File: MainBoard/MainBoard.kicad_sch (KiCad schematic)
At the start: 56 parts, among them J2 Non-Inverting Input, J3 Inverting Input, J4 Output, J5 InvertedOutput, J6 Inverting Input, J7 Non-Inverting Input, J8 Output, J9 InvertedOutput, Q16 BC557, Q32 BC557

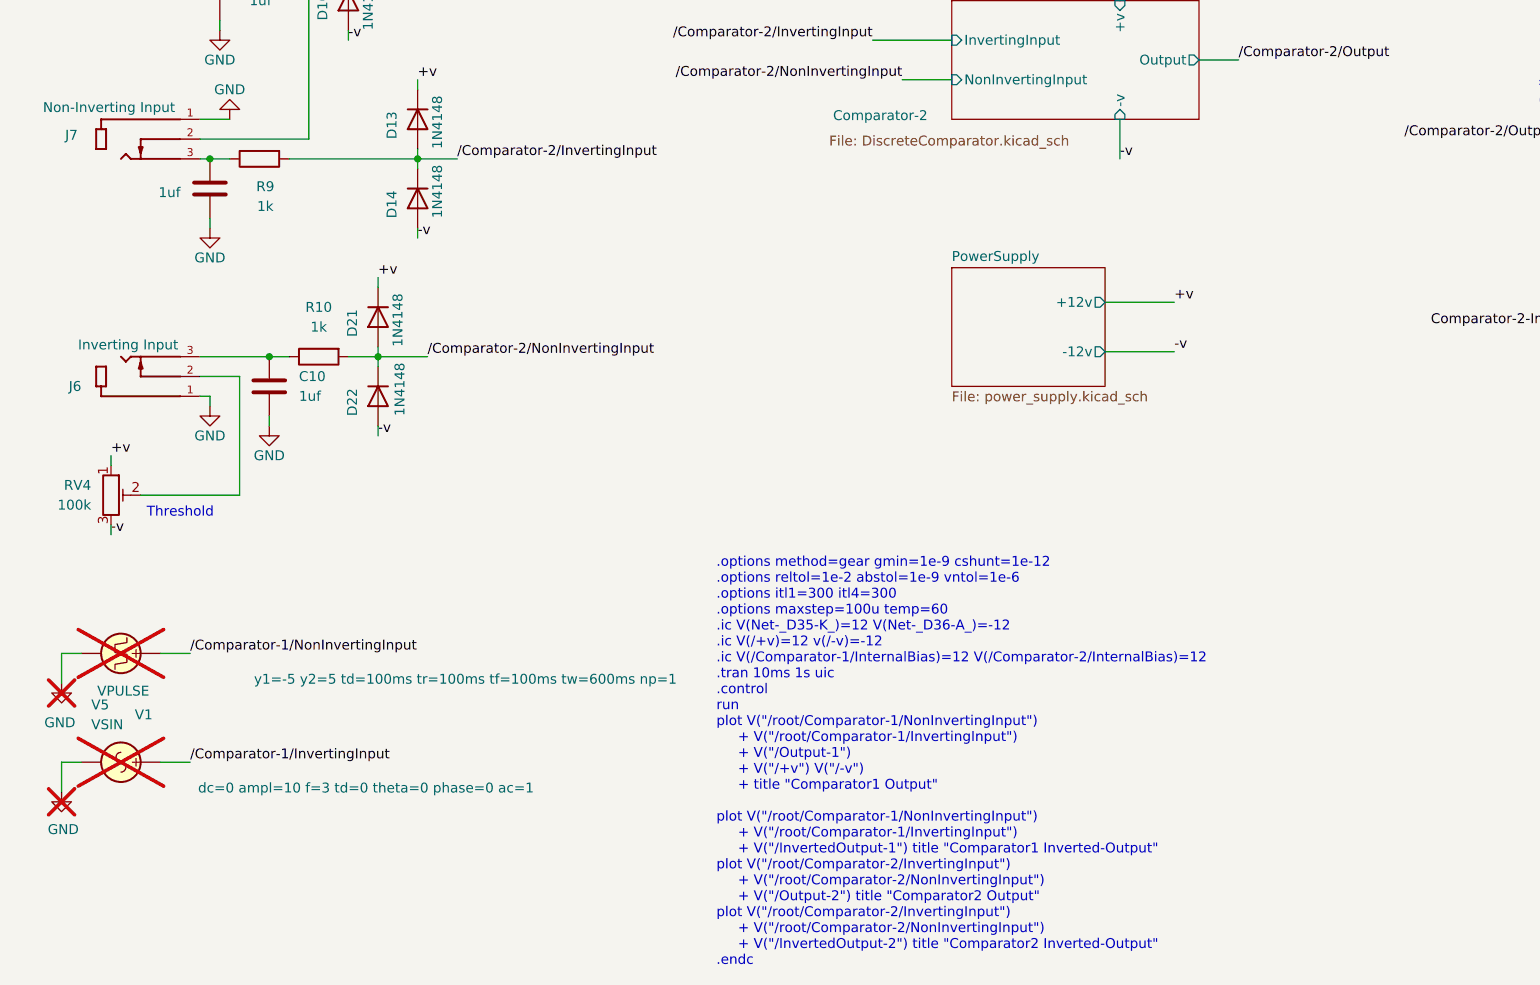
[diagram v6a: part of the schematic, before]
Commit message: updated input signal amplitude -- WIP window comparator testing [i.e, sine wave as threshold currently disabled
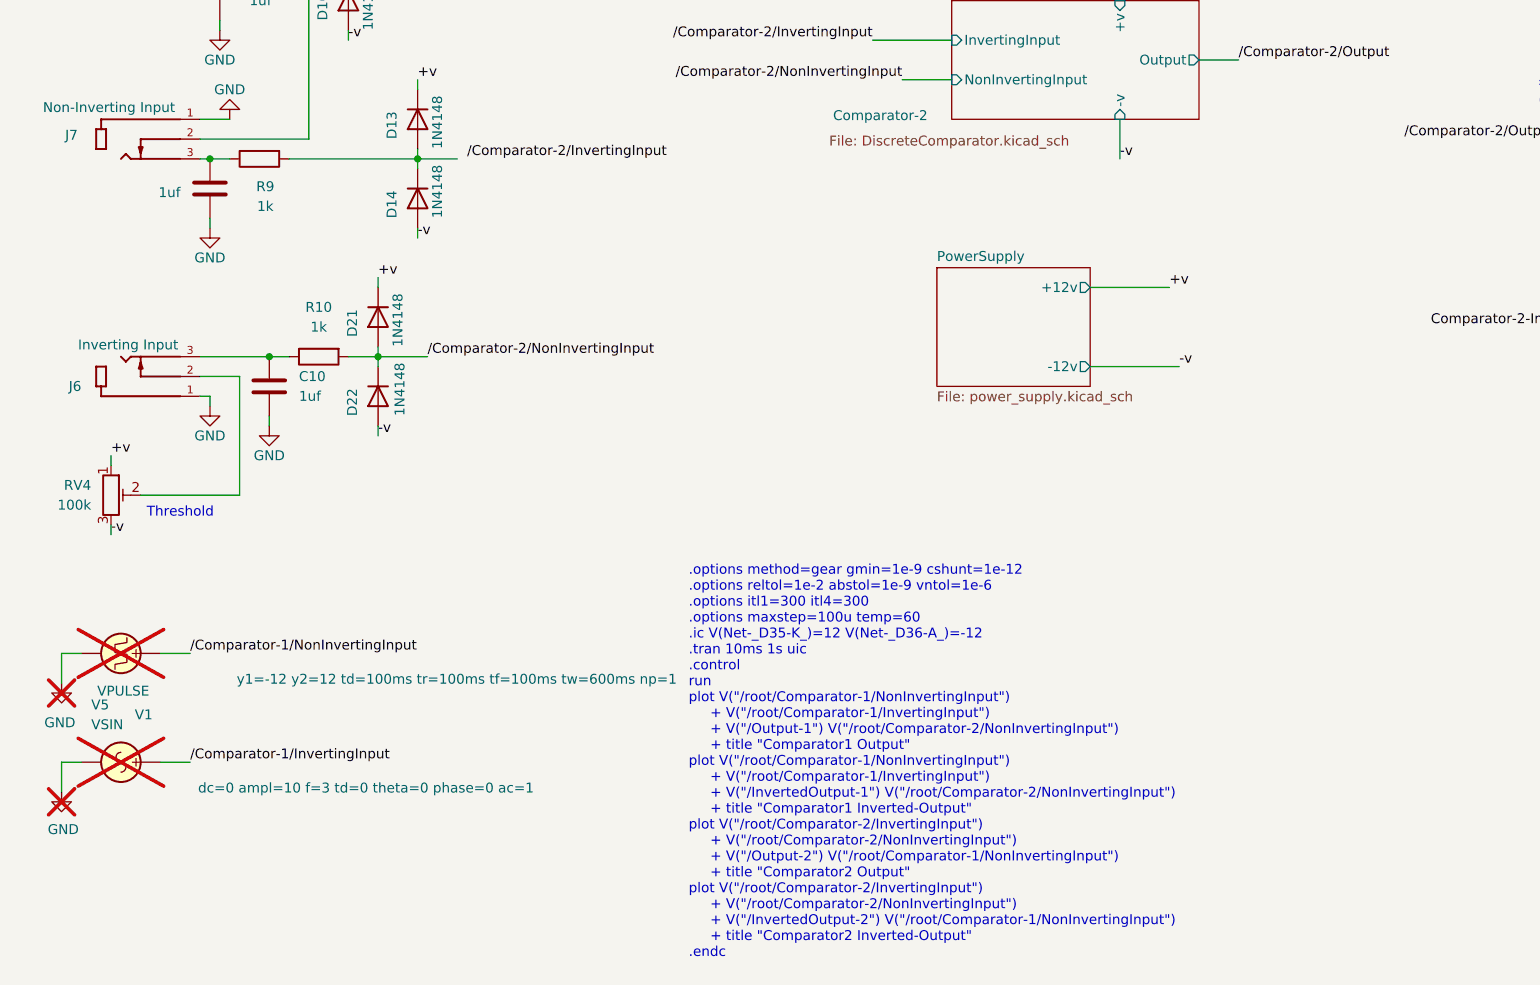
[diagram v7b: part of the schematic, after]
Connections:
- net /Comparator-2/InvertingInput: no longer D13.2 (A), D14.1 (K), R9.2
- new net: D13.2 (A), D14.1 (K), R9.2
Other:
- note added: ".options method=gear gmin=1e-9 cshunt=1e-12 .options reltol=1e-2 abstol=1e-9 vntol=1e-6 .options itl1=300 itl4=300 .options maxstep=100u temp=60 .ic V(Net-_D35-K_)=12 V(Net-_D36-A_)=-12 .tran 10ms 1s uic .control run plot V("/root/Comparator-1/NonInvertingInput") + V("/root/Comparator-1/InvertingInput") + V("/Output-1") V("/root/Comparator-2/NonInvertingInput") + title "Comparator1 Output" plot V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"
- note removed: ".options method=gear gmin=1e-9 cshunt=1e-12 .options reltol=1e-2 abstol=1e-9 vntol=1e-6 .options itl1=300 itl4=300 .options maxstep=100u temp=60 .ic V(Net-_D35-K_)=12 V(Net-_D36-A_)=-12 .ic V(/+v)=12 v(/-v)=-12 .ic V(/Comparator-1/InternalBias)=12 V(/Comparator-2/InternalBias)=12 .tran 10ms 1s uic .control run plot V("/root/Comparator-1/NonInvertingInput") + V("/root/Comparator-1/InvertingInput")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"
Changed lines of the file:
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@@
 		)
 	)
-	(text ".options method=gear gmin=1e-9 cshunt=1e-12 \n.options reltol=1e-2 abstol=1e-9 vntol=1e-6 \n.options itl1=300 itl4=300 \n.options maxstep=100u temp=60\n.ic V(Net-_D35-K_)=12 V(Net-_D36-A_)=-12 \n.ic V(/+v)=12 v(/-v)=-12 \n.ic V(/Comparator-1/InternalBias)=12 V(/Comparator-2/InternalBias)=12\n.tran 10ms 1s uic\n.control\nrun\nplot V(\"/root/Comparator-1/NonInvertingInput\") \n     + V(\"/root/Comparator-1/InvertingInput\") \n     + V(\"/Output-1\")\n     + V(\"/+v\") V(\"/-v\")\n     + title \"Comparator1 Output\" \n    \nplot V(\"/root/Comparator-1/NonInvertingInput\")\n     + V(\"/root/Comparator-1/InvertingInput\")\n     + V(\"/InvertedOutput-1\") title \"Comparator1 Inverted-Output\"\nplot V(\"/root/Comparator-2/InvertingInput\") \n     + V(\"/root/Comparator-2/NonInvertingInput\")   \n     + V(\"/Output-2\") title \"Comparator2 Output\" \nplot V(\"/root/Comparator-2/InvertingInput\")\n     + V(\"/root/Comparator-2/NonInvertingInput\") \n     + V(\"/InvertedOutput-2\") title \"Comparator2 Inverted-Output\"\n.endc"
+	(text ".options method=gear gmin=1e-9 cshunt=1e-12 \n.options reltol=1e-2 abstol=1e-9 vntol=1e-6 \n.options itl1=300 itl4=300 \n.options maxstep=100u temp=60\n.ic V(Net-_D35-K_)=12 V(Net-_D36-A_)=-12 \n.tran 10ms 1s uic\n.control\nrun\nplot V(\"/root/Comparator-1/NonInvertingInput\") \n     + V(\"/root/Comparator-1/InvertingInput\") \n     + V(\"/Output-1\") V(\"/root/Comparator-2/NonInvertingInput\")\n     + title \"Comparator1 Output\" \nplot V(\"/root/Comparator-1/NonInvertingInput\")\n     + V(\"/root/Comparator-1/InvertingInput\")\n     + V(\"/InvertedOutput-1\") V(\"/root/Comparator-2/NonInvertingInput\")\n     + title \"Comparator1 Inverted-Output\"\nplot V(\"/root/Comparator-2/InvertingInput\") \n     + V(\"/root/Comparator-2/NonInvertingInput\")   \n     + V(\"/Output-2\") V(\"/root/Comparator-1/NonInvertingInput\") \n     + title \"Comparator2 Output\" \nplot V(\"/root/Comparator-2/InvertingInput\")\n     + V(\"/root/Comparator-2/NonInvertingInput\") \n     + V(\"/InvertedOutput-2\") V(\"/root/Comparator-1/NonInvertingInput\") \n     + title \"Comparator2 Inverted-Output\"\n.endc"
 		(exclude_from_sim no)
-		(at 105.664 168.91 0)
+		(at 102.108 168.91 0)
 		(effects
 			(font
@@
 	(wire
 		(pts
+			(xy 153.67 107.95) (xy 163.83 107.95)
+		)
+		(stroke
+			(width 0)
+			(type default)
+		)
+	)
+	(wire
+		(pts
 			(xy 58.42 55.88) (xy 58.42 57.15)
 		)
@@
 	(wire
 		(pts
-			(xy 40.64 123.19) (xy 40.64 121.92)
+			(xy 153.67 118.11) (xy 165.1 118.11)
 		)
 		(stroke
@@
 	(wire
 		(pts
-			(xy 34.29 154.94) (xy 38.1 154.94)
+			(xy 40.64 123.19) (xy 40.64 121.92)
 		)
 		(stroke
@@
 	(wire
 		(pts
-			(xy 63.5 27.94) (xy 63.5 29.21)
+			(xy 34.29 154.94) (xy 38.1 154.94)
 		)
 		(stroke
@@
 	(wire
 		(pts
-			(xy 27.94 129.54) (xy 27.94 130.81)
+			(xy 63.5 27.94) (xy 63.5 29.21)
 		)
 		(stroke
@@
 	(wire
 		(pts
-			(xy 217.17 78.74) (xy 217.17 81.28)
+			(xy 27.94 129.54) (xy 27.94 130.81)
 		)
 		(stroke
@@
 	(wire
 		(pts
-			(xy 155.575 109.855) (xy 164.465 109.855)
+			(xy 217.17 78.74) (xy 217.17 81.28)
 		)
 		(stroke
@@
 	(wire
 		(pts
-			(xy 155.575 116.205) (xy 164.465 116.205)
-		)
-		(stroke
-			(width 0)
-			(type default)
-		)
-	)
-	(wire
-		(pts
 			(xy 44.45 119.38) (xy 39.37 119.38)
 		)
@@
 	)
 	(label "+v"
-		(at 164.465 109.855 0)
+		(at 163.83 107.95 0)
 		(effects
 			(font
@@
 	)
 	(label "{slash}Comparator-2{slash}InvertingInput"
-		(at 72.39 91.44 0)
+		(at 73.66 91.44 0)
 		(effects
 			(font
@@
 	)
 	(label "-v"
-		(at 164.465 116.205 0)
+		(at 165.1 118.11 0)
 		(effects
 			(font
@@
 			)
 		)
-		(property "Sim.Params" "Rtot=100k w=0.3"
+		(property "Sim.Params" "Rtot=100k w=0.7"
 			(at 27.94 134.62 0)
 			(effects
@@
 			)
 		)
-		(property "Sim.Params" "y1=-5 y2=5 td=100ms tr=100ms tf=100ms tw=600ms np=1"
+		(property "Sim.Params" "y1=-12  y2=12 td=100ms tr=100ms tf=100ms tw=600ms np=1"
 			(at 100.584 158.242 90)
 			(effects
@@
 			)
 		)
-		(property "Sim.Params" "Rtot=100k w=0.7"
+		(property "Sim.Params" "Rtot=100k w=0.6"
 			(at 29.21 46.99 0)
 			(effects
@@
 		(mirror x)
 		(unit 1)
-		(exclude_from_sim no)
+		(exclude_from_sim yes)
 		(in_bom no)
 		(on_board no)
@@
 	)
 	(sheet
-		(at 135.89 105.41)
+		(at 133.985 105.41)
 		(size 19.685 15.24)
 		(exclude_from_sim no)
@@
 		)
 		(property "Sheetname" "PowerSupply"
-			(at 135.89 104.6984 0)
+			(at 133.985 104.6984 0)
 			(effects
 				(font
@@
 		)
 		(property "Sheetfile" "power_supply.kicad_sch"
-			(at 135.89 121.2346 0)
+			(at 133.985 121.2346 0)
 			(effects
 				(font
@@
 		)
 		(pin "+12v" output
-			(at 155.575 109.855 0)
+			(at 153.67 107.95 0)
 			(effects
 				(font
@@
 		)
 		(pin "-12v" output
-			(at 155.575 116.205 0)
+			(at 153.67 118.11 0)
 			(effects
 				(font
